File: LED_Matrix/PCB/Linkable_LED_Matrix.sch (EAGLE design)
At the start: 9 parts

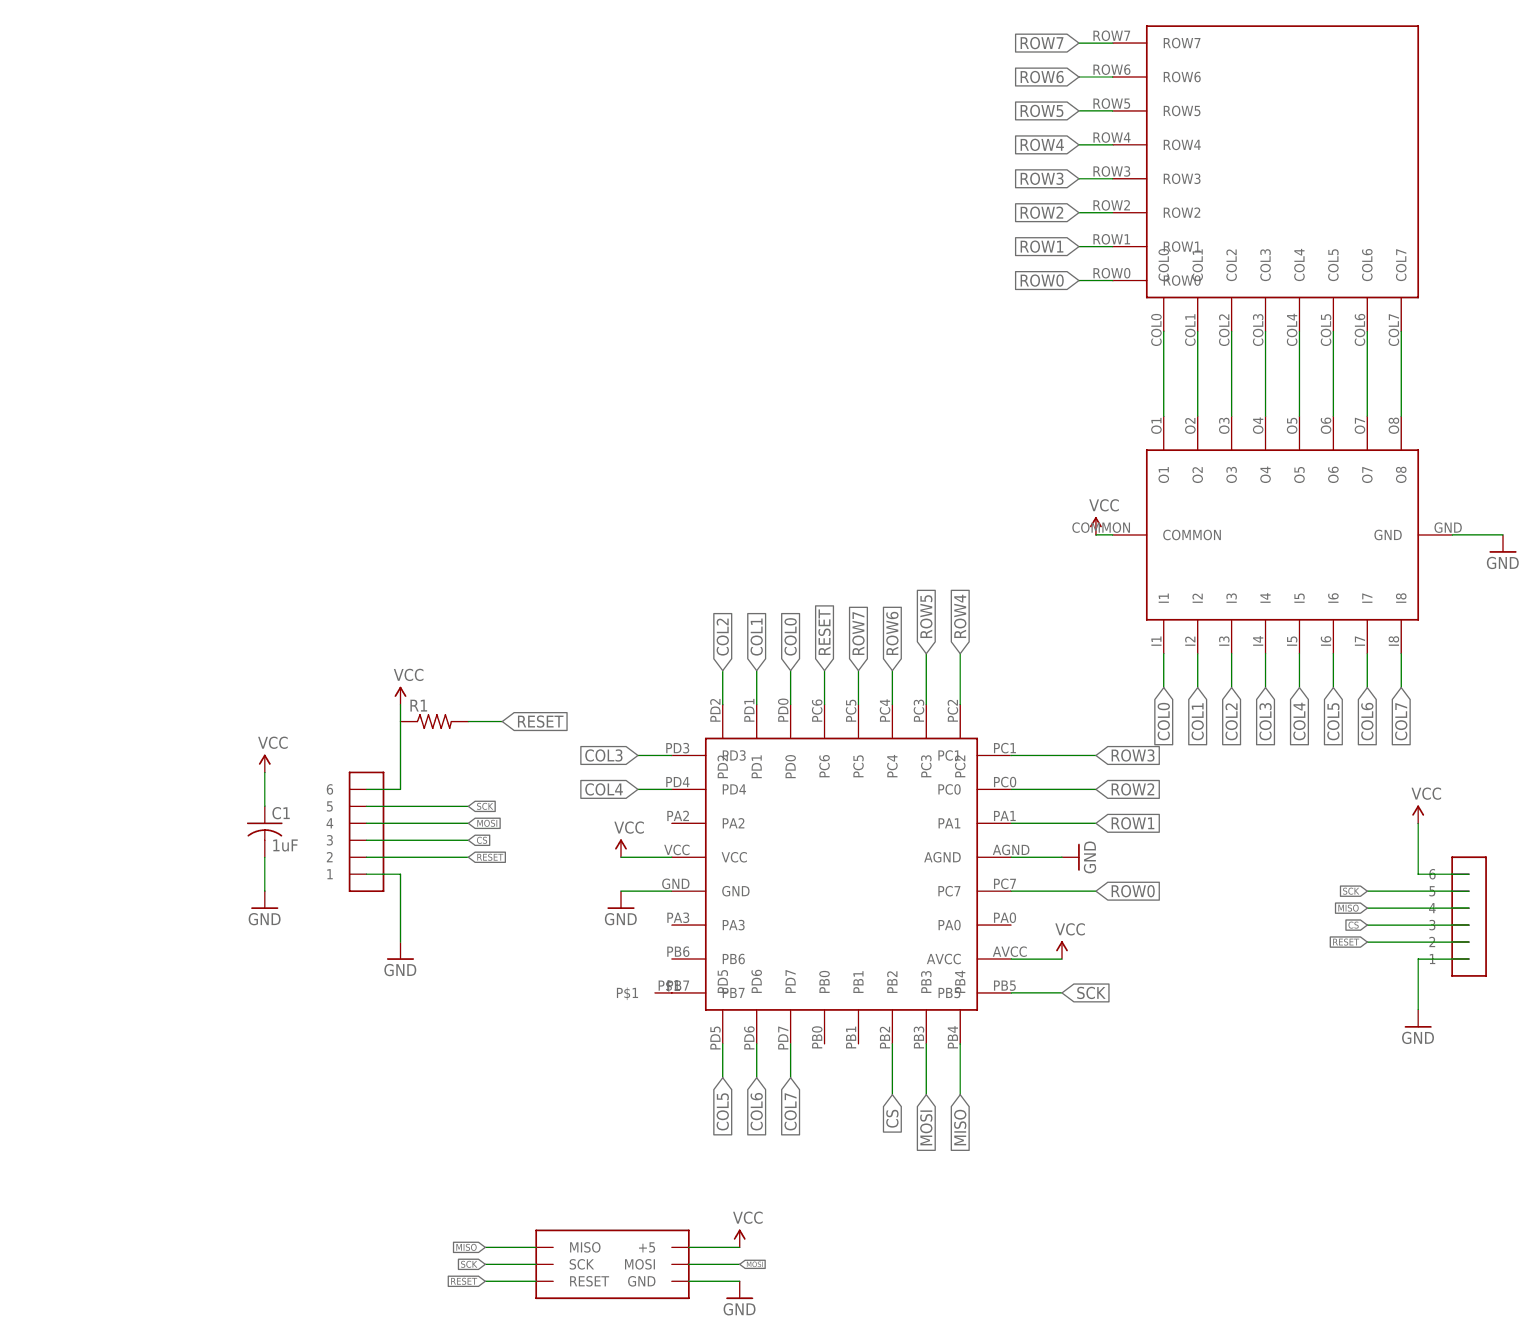
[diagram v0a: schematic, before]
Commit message: led - matrix - new mounting holes, rerouted...
Added new mounting hole strategy - holes are 0.125" unplated, and can mount
with m2.5 screws, or plastic pressfit standoffs.

Silikscreen cleaned up - all labels moved away from vias, and placed upright.
Added clear labelling for all parts, and put horizontal lines across the board
showing chaining connectivity.

Put ATTINY's decoupling cap closer to part.

12 mil traces for passthru VCC/GND/SCLK.  All others 8mil.

Removed unused test pad.
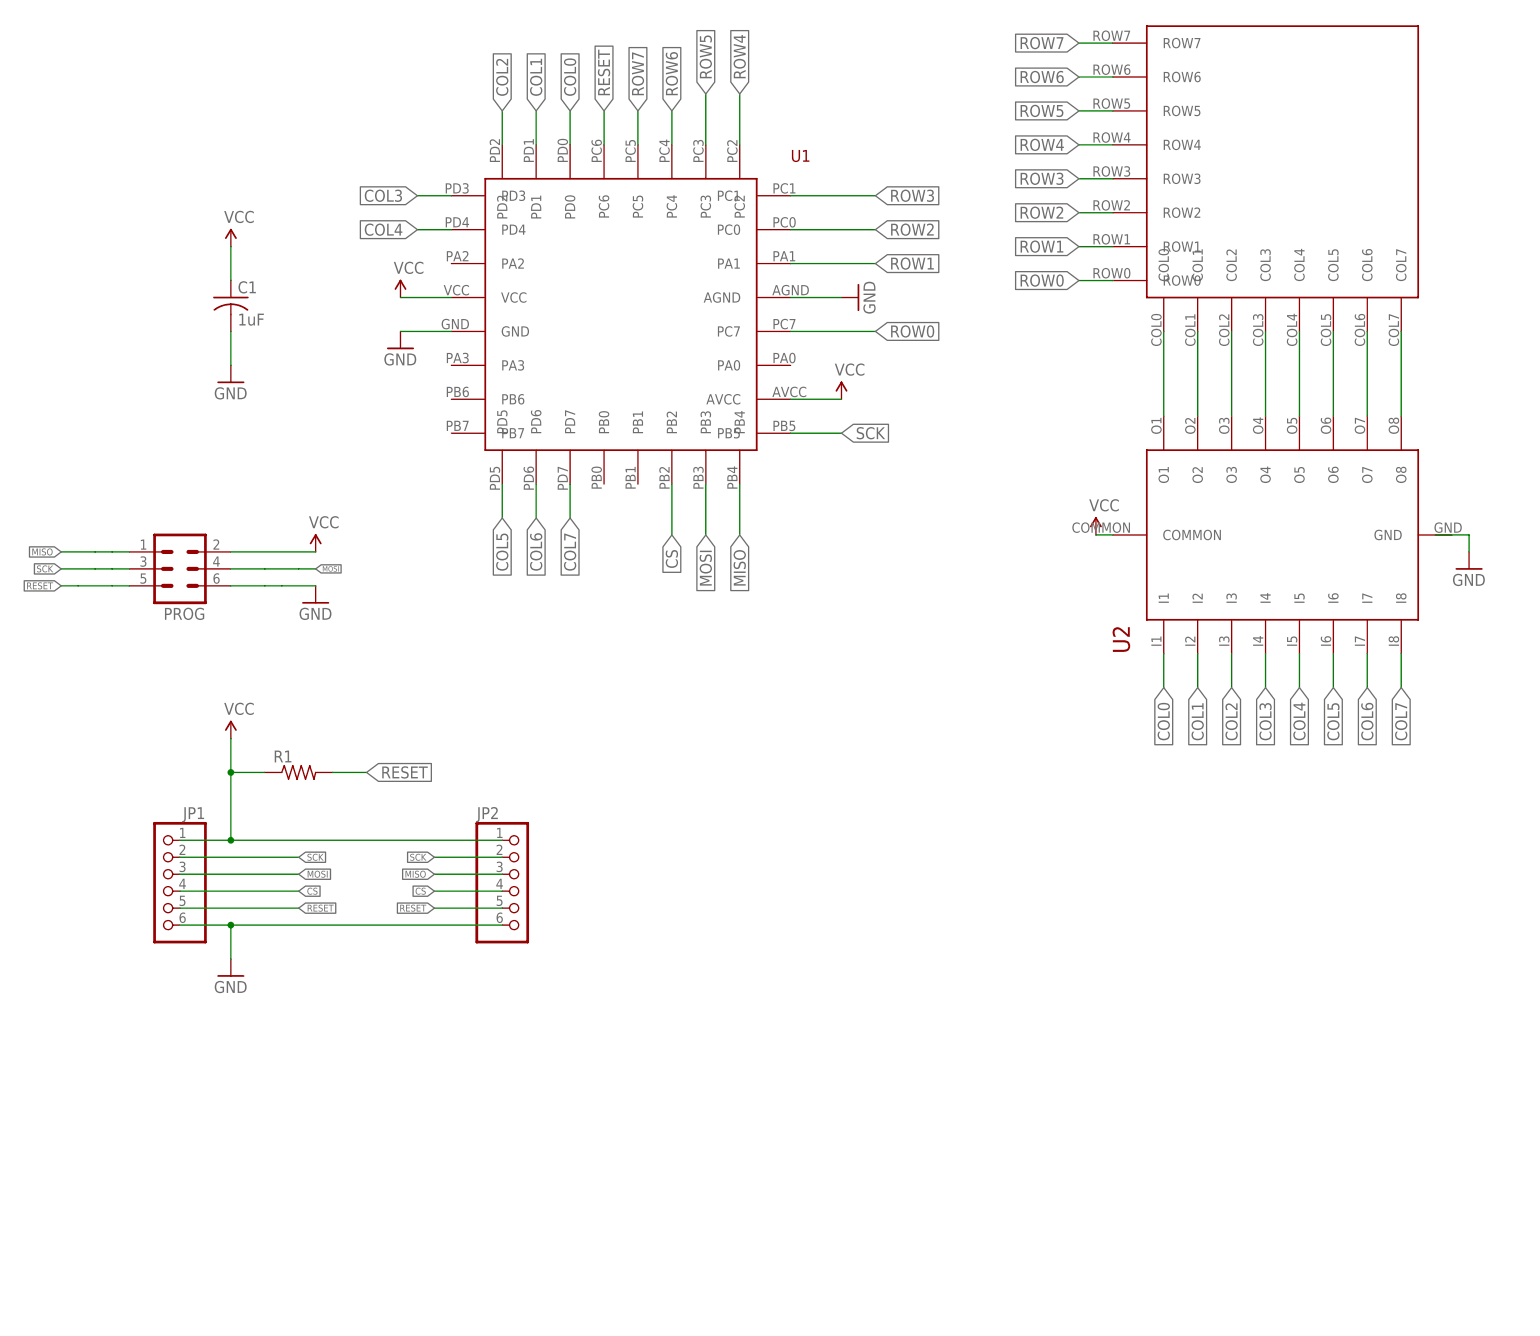
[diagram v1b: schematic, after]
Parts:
- removed U$1: ATTINY48, ScottSilver:ATTINY48
- removed U$2: ULN2803AFWG, ScottSilver:ULN2803AFWG
- removed U$3: 8X8_LED_MATRIX, ScottSilver:8X8_LED_MATRIX
- removed U$5: 1X1MM_PAD, ScottSilver:1X1MM_PAD
- removed U$6, U$7: DIP1X6MALE, ScottSilver:DIP1X6MALE
- removed U$9: DIP2X3MALE, ScottSilver:DIP2X3MALE
- added JP1, JP2: (no value), raspberrystem:PINHD-1X6
- added LEDMATRIX: 8X8_LED_MATRIX, raspberrystem:8X8_LED_MATRIX
- added PROG: (no value), raspberrystem:MA03-2
- added U1: ATTINY48, raspberrystem:ATTINY48
- added U2: ULN2803AFWG, raspberrystem:ULN2803AFWG
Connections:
- removed net N$13: U$1.PB7, U$5.P$1
- net COL0: now also U1.PD0, U2.I1; no longer U$1.PD0, U$2.I1
- net COL1: now also U1.PD1, U2.I2; no longer U$1.PD1, U$2.I2
- net COL2: now also U1.PD2, U2.I3; no longer U$1.PD2, U$2.I3
- net COL3: now also U1.PD3, U2.I4; no longer U$1.PD3, U$2.I4
- net COL4: now also U1.PD4, U2.I5; no longer U$1.PD4, U$2.I5
- net COL5: now also U1.PD5, U2.I6; no longer U$1.PD5, U$2.I6
- net COL6: now also U1.PD6, U2.I7; no longer U$1.PD6, U$2.I7
- net COL7: now also U1.PD7, U2.I8; no longer U$1.PD7, U$2.I8
- net CS: now also JP1.4, JP2.4, U1.PB2; no longer U$1.PB2, U$6.3, U$7.3
- net GND: now also JP1.6, JP2.6, PROG.6, U1.AGND, U1.GND; no longer U$1.AGND, U$1.GND, U$2.GND, U$6.1, U$7.1, U$9.GND
- net MISO: now also JP2.3, PROG.1, U1.PB4; no longer U$1.PB4, U$7.4, U$9.MISO
- net MOSI: now also JP1.3, PROG.4, U1.PB3; no longer U$1.PB3, U$6.4, U$9.MOSI
- net N$1: now also LEDMATRIX.COL0, U2.O1; no longer U$2.O1, U$3.COL0
- net N$2: now also LEDMATRIX.COL1, U2.O2; no longer U$2.O2, U$3.COL1
- net N$3: now also LEDMATRIX.COL2, U2.O3; no longer U$2.O3, U$3.COL2
- net N$4: now also LEDMATRIX.COL3, U2.O4; no longer U$2.O4, U$3.COL3
- net N$5: now also LEDMATRIX.COL4, U2.O5; no longer U$2.O5, U$3.COL4
- net N$6: now also LEDMATRIX.COL5, U2.O6; no longer U$2.O6, U$3.COL5
- net N$7: now also LEDMATRIX.COL6, U2.O7; no longer U$2.O7, U$3.COL6
- net N$8: now also LEDMATRIX.COL7, U2.O8; no longer U$2.O8, U$3.COL7
- net RESET: now also JP1.5, JP2.5, PROG.5, U1.PC6; no longer U$1.PC6, U$6.2, U$7.2, U$9.RESET
- net ROW0: now also LEDMATRIX.ROW0, U1.PC7; no longer U$1.PC7, U$3.ROW0
- net ROW1: now also LEDMATRIX.ROW1, U1.PA1; no longer U$1.PA1, U$3.ROW1
- net ROW2: now also LEDMATRIX.ROW2, U1.PC0; no longer U$1.PC0, U$3.ROW2
- net ROW3: now also LEDMATRIX.ROW3, U1.PC1; no longer U$1.PC1, U$3.ROW3
- net ROW4: now also LEDMATRIX.ROW4, U1.PC2; no longer U$1.PC2, U$3.ROW4
- net ROW5: now also LEDMATRIX.ROW5, U1.PC3; no longer U$1.PC3, U$3.ROW5
- net ROW6: now also LEDMATRIX.ROW6, U1.PC4; no longer U$1.PC4, U$3.ROW6
- net ROW7: now also LEDMATRIX.ROW7, U1.PC5; no longer U$1.PC5, U$3.ROW7
- net SCK: now also JP1.2, JP2.2, PROG.3, U1.PB5; no longer U$1.PB5, U$6.5, U$7.5, U$9.SCK
- net VCC: now also JP1.1, JP2.1, PROG.2, U1.AVCC, U1.VCC, U2.COMMON; no longer U$1.AVCC, U$1.VCC, U$2.COMMON, U$6.6, U$7.6, U$9.+5
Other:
- moved on the sheet: C1, R1
